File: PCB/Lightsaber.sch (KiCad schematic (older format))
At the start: 10 parts, among them Q1 SS8050, Q2 SS8050, Q3 SS8050, SW1 SW_Push

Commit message: updated ss8050 pin numbering
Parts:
- D2: footprint (none) -> Connector_PinHeader_2.54mm:PinHeader_1x04_P2.54mm_Vertical
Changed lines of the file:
@@
 F 0 "D2" V 10196 820 50  0000 R CNN
 F 1 "LED_ARGB" V 10105 820 50  0000 R CNN
-F 2 "" H 10150 1100 50  0001 C CNN
+F 2 "Connector_PinHeader_2.54mm:PinHeader_1x04_P2.54mm_Vertical" H 10150 1100 50  0001 C CNN
 F 3 "~" H 10150 1100 50  0001 C CNN
 	1    10150 1150

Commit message: update
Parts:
- added BT?: Battery_Cell, symbol Device:Battery_Cell
- added C?: C, symbol Device:C
- added F?: Fuse, symbol Device:Fuse
- added R?: 100, symbol Device:R
- added U?: DW01A, symbol Lightsaber_custom:DW01A
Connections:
- new net: BT?.1 (+), F?.2
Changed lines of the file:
@@
 Wire Wire Line
 	9800 3250 9800 3400
+$Comp
+L Device:Battery_Cell BT?
+U 1 1 631E3320
+P 800 1800
+F 0 "BT?" H 918 1896 50  0000 L CNN
+F 1 "Battery_Cell" H 918 1805 50  0000 L CNN
+F 2 "" V 800 1860 50  0001 C CNN
+F 3 "~" V 800 1860 50  0001 C CNN
+	1    800  1800
+	1    0    0    -1
+$EndComp
+$Comp
+L Device:Fuse F?
+U 1 1 631E4D50
+P 1200 1550
+F 0 "F?" V 1003 1550 50  0000 C CNN
+F 1 "Fuse" V 1094 1550 50  0000 C CNN
+F 2 "" V 1130 1550 50  0001 C CNN
+F 3 "~" H 1200 1550 50  0001 C CNN
+	1    1200 1550
+	0    1    1    0
+$EndComp
+Wire Wire Line
+	800  1600 800  1550
+Wire Wire Line
+	800  1550 1050 1550
+$Comp
+L Lightsaber_custom:DW01A U?
+U 1 1 631E6E9D
+P 2800 1150
+F 0 "U?" H 2750 1215 50  0000 C CNN
+F 1 "DW01A" H 2750 1124 50  0000 C CNN
+F 2 "" H 2750 1200 50  0001 C CNN
+F 3 "" H 2750 1200 50  0001 C CNN
+	1    2800 1150
+	1    0    0    -1
+$EndComp
+$Comp
+L Device:R R?
+U 1 1 631E7B9E
+P 1900 1350
+F 0 "R?" V 1693 1350 50  0000 C CNN
+F 1 "100" V 1784 1350 50  0000 C CNN
+F 2 "" V 1830 1350 50  0001 C CNN
+F 3 "~" H 1900 1350 50  0001 C CNN
+	1    1900 1350
+	0    1    1    0
+$EndComp
+$Comp
+L Device:C C?
+U 1 1 631E8406
+P 2100 1650
+F 0 "C?" H 2215 1696 50  0000 L CNN
+F 1 "C" H 2215 1605 50  0000 L CNN
+F 2 "" H 2138 1500 50  0001 C CNN
+F 3 "~" H 2100 1650 50  0001 C CNN
+	1    2100 1650
+	1    0    0    -1
+$EndComp
 $EndSCHEMATC

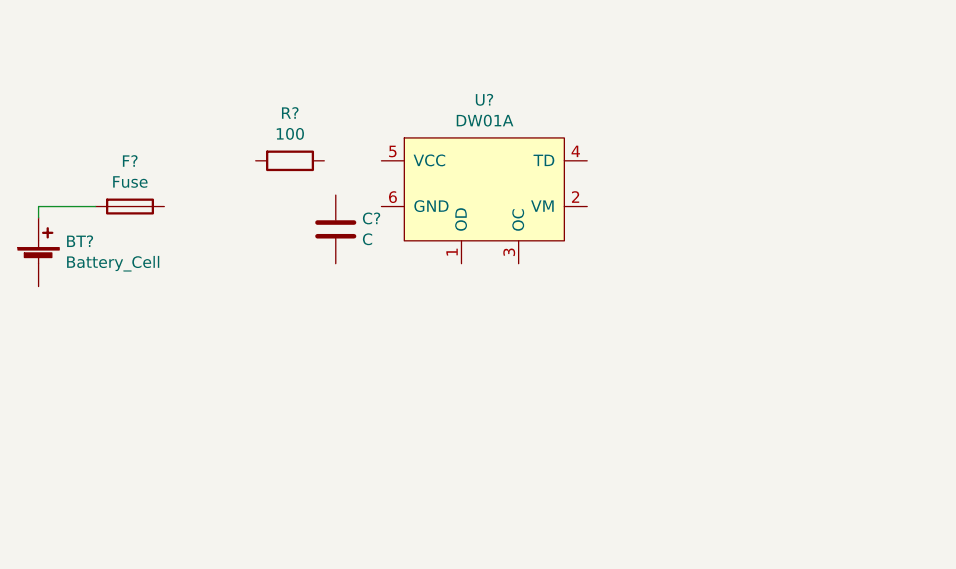
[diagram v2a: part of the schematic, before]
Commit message: battery protection added
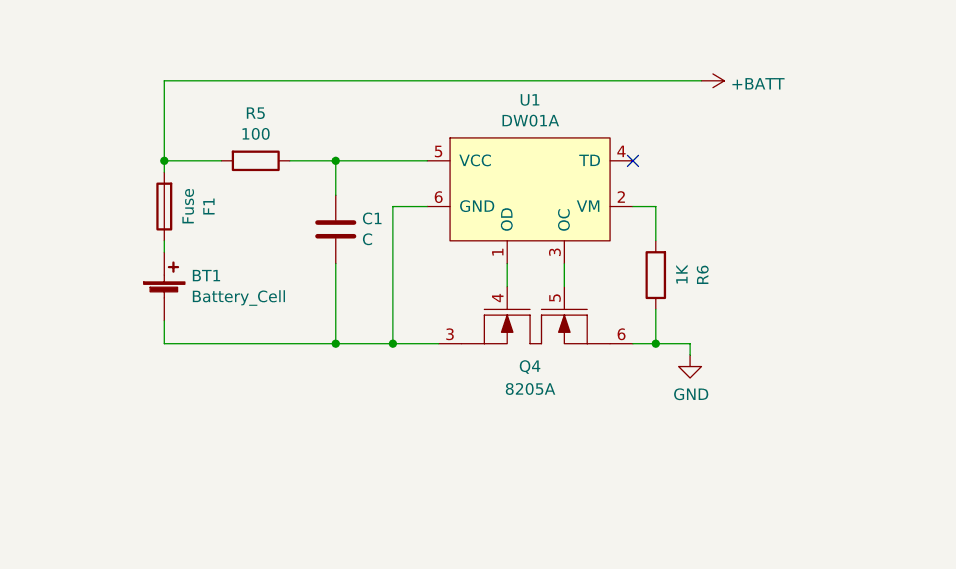
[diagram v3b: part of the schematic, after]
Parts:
- added Q4: 8205A, Package_SO:TSSOP-8_4.4x3mm_P0.65mm, symbol Lightsaber_custom:8205A
- added R6: 1K, Resistor_SMD:R_0402_1005Metric, symbol Device:R
- R5: renamed from R?; footprint (none) -> Resistor_SMD:R_0402_1005Metric
- U1: renamed from U?; footprint (none) -> Package_TO_SOT_SMD:SOT-23-6_Handsoldering
- gave numbers to parts that had none: 3
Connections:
- net GND: now also Q4.6 (S2), R6.1
- net at BT1.1 (+): now also F1.1; no longer F1.2
- net at BT1.2 (-): now also C1.2, U1.6 (GND), Q4.3 (S1)
- net at U1.1 (OD): now also Q4.4 (G1)
- net at U1.2 (VM): now also R6.2
- net at U1.3 (OC): now also Q4.5 (G2)
- net at U1.5 (VCC): now also C1.1, R5.1
- net +BATT: now reaches R5.2
- net +BATT: now also F1.2
- no-connect marks 0 -> 1
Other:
- moved on the sheet: BT1, F1, R5, U1
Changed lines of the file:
@@
 	9800 3250 9800 3400
 $Comp
-L Device:Battery_Cell BT?
+L Device:Battery_Cell BT1
 U 1 1 631E3320
-P 800 1800
-F 0 "BT?" H 918 1896 50  0000 L CNN
-F 1 "Battery_Cell" H 918 1805 50  0000 L CNN
-F 2 "" V 800 1860 50  0001 C CNN
-F 3 "~" V 800 1860 50  0001 C CNN
-	1    800  1800
+P 1350 1950
+F 0 "BT1" H 1468 2046 50  0000 L CNN
+F 1 "Battery_Cell" H 1468 1955 50  0000 L CNN
+F 2 "" V 1350 2010 50  0001 C CNN
+F 3 "~" V 1350 2010 50  0001 C CNN
+	1    1350 1950
 	1    0    0    -1
 $EndComp
 $Comp
-L Device:Fuse F?
+L Device:Fuse F1
 U 1 1 631E4D50
-P 1200 1550
-F 0 "F?" V 1003 1550 50  0000 C CNN
-F 1 "Fuse" V 1094 1550 50  0000 C CNN
-F 2 "" V 1130 1550 50  0001 C CNN
-F 3 "~" H 1200 1550 50  0001 C CNN
-	1    1200 1550
-	0    1    1    0
+P 1350 1550
+F 0 "F1" V 1153 1550 50  0000 C CNN
+F 1 "Fuse" V 1244 1550 50  0000 C CNN
+F 2 "" V 1280 1550 50  0001 C CNN
+F 3 "~" H 1350 1550 50  0001 C CNN
+	1    1350 1550
+	-1   0    0    1
 $EndComp
-Wire Wire Line
-	800  1600 800  1550
-Wire Wire Line
-	800  1550 1050 1550
 $Comp
-L Lightsaber_custom:DW01A U?
+L Lightsaber_custom:DW01A U1
 U 1 1 631E6E9D
-P 2800 1150
-F 0 "U?" H 2750 1215 50  0000 C CNN
-F 1 "DW01A" H 2750 1124 50  0000 C CNN
-F 2 "" H 2750 1200 50  0001 C CNN
-F 3 "" H 2750 1200 50  0001 C CNN
-	1    2800 1150
+P 3000 1150
+F 0 "U1" H 2950 1215 50  0000 C CNN
+F 1 "DW01A" H 2950 1124 50  0000 C CNN
+F 2 "Package_TO_SOT_SMD:SOT-23-6_Handsoldering" H 2950 1200 50  0001 C CNN
+F 3 "" H 2950 1200 50  0001 C CNN
+	1    3000 1150
 	1    0    0    -1
 $EndComp
 $Comp
-L Device:R R?
+L Device:R R5
 U 1 1 631E7B9E
-P 1900 1350
-F 0 "R?" V 1693 1350 50  0000 C CNN
-F 1 "100" V 1784 1350 50  0000 C CNN
-F 2 "" V 1830 1350 50  0001 C CNN
-F 3 "~" H 1900 1350 50  0001 C CNN
-	1    1900 1350
+P 1750 1350
+F 0 "R5" V 1543 1350 50  0000 C CNN
+F 1 "100" V 1634 1350 50  0000 C CNN
+F 2 "Resistor_SMD:R_0402_1005Metric" V 1680 1350 50  0001 C CNN
+F 3 "~" H 1750 1350 50  0001 C CNN
+	1    1750 1350
 	0    1    1    0
 $EndComp
 $Comp
-L Device:C C?
+L Device:C C1
 U 1 1 631E8406
 P 2100 1650
-F 0 "C?" H 2215 1696 50  0000 L CNN
+F 0 "C1" H 2215 1696 50  0000 L CNN
 F 1 "C" H 2215 1605 50  0000 L CNN
 F 2 "" H 2138 1500 50  0001 C CNN
@@
 	1    0    0    -1
 $EndComp
+$Comp
+L power:GND #PWR0101
+U 1 1 631F39B5
+P 3650 2200
+F 0 "#PWR0101" H 3650 1950 50  0001 C CNN
+F 1 "GND" H 3655 2027 50  0000 C CNN
+F 2 "" H 3650 2200 50  0001 C CNN
+F 3 "" H 3650 2200 50  0001 C CNN
+	1    3650 2200
+	1    0    0    -1
+$EndComp
+$Comp
+L Lightsaber_custom:8205A Q4
+U 1 1 631FA975
+P 3000 1700
+F 0 "Q4" H 2950 1150 50  0000 C CNN
+F 1 "8205A" H 2950 1050 50  0000 C CNN
+F 2 "Package_SO:TSSOP-8_4.4x3mm_P0.65mm" H 3000 1700 50  0001 C CNN
+F 3 "" H 3000 1700 50  0001 C CNN
+	1    3000 1700
+	1    0    0    -1
+$EndComp
+Wire Wire Line
+	2850 1800 2850 1900
+Wire Wire Line
+	3100 1800 3100 1900
+Wire Wire Line
+	2500 1550 2350 1550
+Wire Wire Line
+	2350 1550 2350 2150
+Connection ~ 2350 2150
+Wire Wire Line
+	2350 2150 2550 2150
+Wire Wire Line
+	2500 1350 2100 1350
+Wire Wire Line
+	2100 1500 2100 1350
+Connection ~ 2100 1350
+Wire Wire Line
+	2100 1350 1900 1350
+Wire Wire Line
+	2100 1800 2100 2150
+Wire Wire Line
+	2100 2150 2350 2150
+Wire Wire Line
+	1350 1350 1350 1400
+Wire Wire Line
+	1350 1700 1350 1750
+Wire Wire Line
+	1350 1350 1600 1350
+Wire Wire Line
+	1350 2050 1350 2150
+Connection ~ 2100 2150
+Wire Wire Line
+	3650 2200 3650 2150
+Wire Wire Line
+	1350 2150 2100 2150
+$Comp
+L Device:R R6
+U 1 1 6320AF5C
+P 3500 1850
+F 0 "R6" V 3293 1850 50  0000 C CNN
+F 1 "1K" V 3384 1850 50  0000 C CNN
+F 2 "Resistor_SMD:R_0402_1005Metric" V 3430 1850 50  0001 C CNN
+F 3 "~" H 3500 1850 50  0001 C CNN
+	1    3500 1850
+	-1   0    0    1
+$EndComp
+Wire Wire Line
+	3400 2150 3500 2150
+Wire Wire Line
+	3500 2000 3500 2150
+Connection ~ 3500 2150
+Wire Wire Line
+	3500 2150 3650 2150
+Wire Wire Line
+	3500 1700 3500 1550
+Wire Wire Line
+	3500 1550 3400 1550
+NoConn ~ 3400 1350
+Wire Wire Line
+	1350 1350 1350 1000
+Wire Wire Line
+	1350 1000 3700 1000
+Connection ~ 1350 1350
+$Comp
+L power:+BATT #PWR0102
+U 1 1 6321023C
+P 3700 1000
+F 0 "#PWR0102" H 3700 850 50  0001 C CNN
+F 1 "+BATT" V 3715 1128 50  0000 L CNN
+F 2 "" H 3700 1000 50  0001 C CNN
+F 3 "" H 3700 1000 50  0001 C CNN
+	1    3700 1000
+	0    1    1    0
+$EndComp
 $EndSCHEMATC

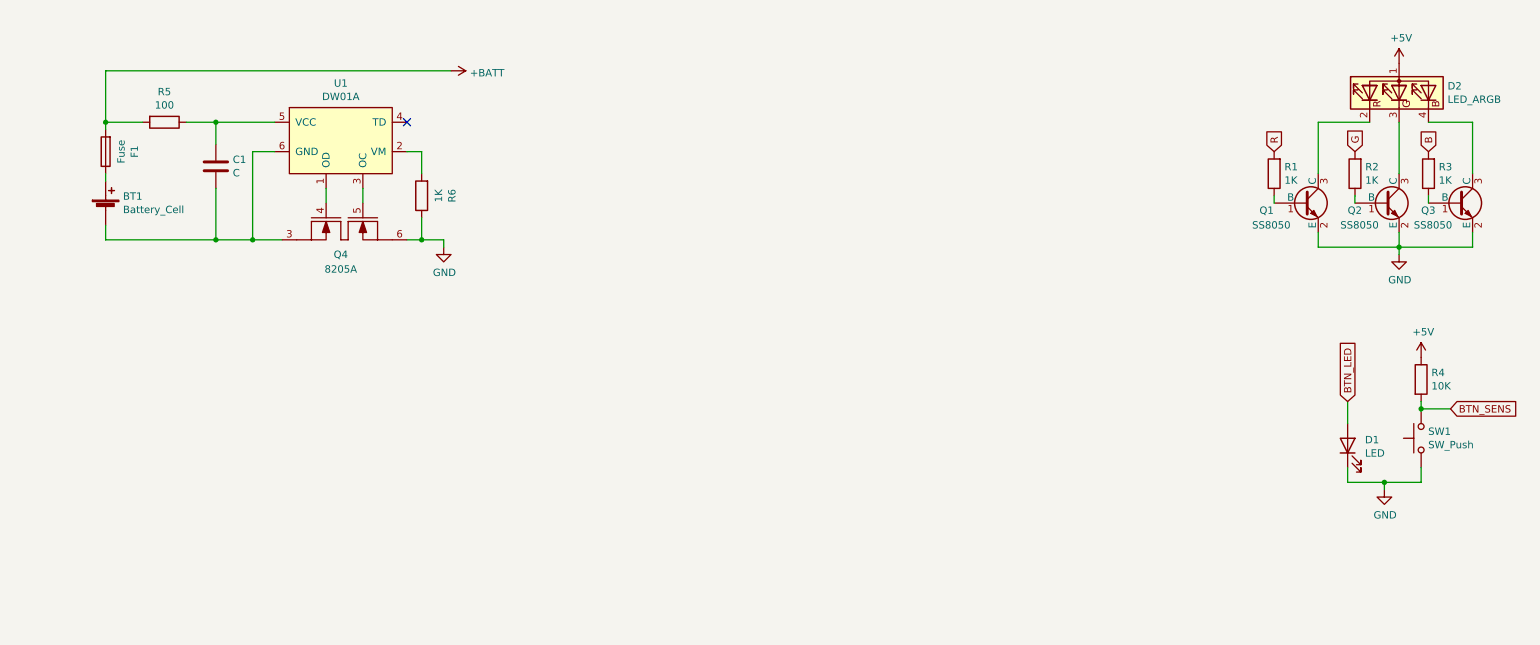
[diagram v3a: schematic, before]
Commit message: charging circuit added
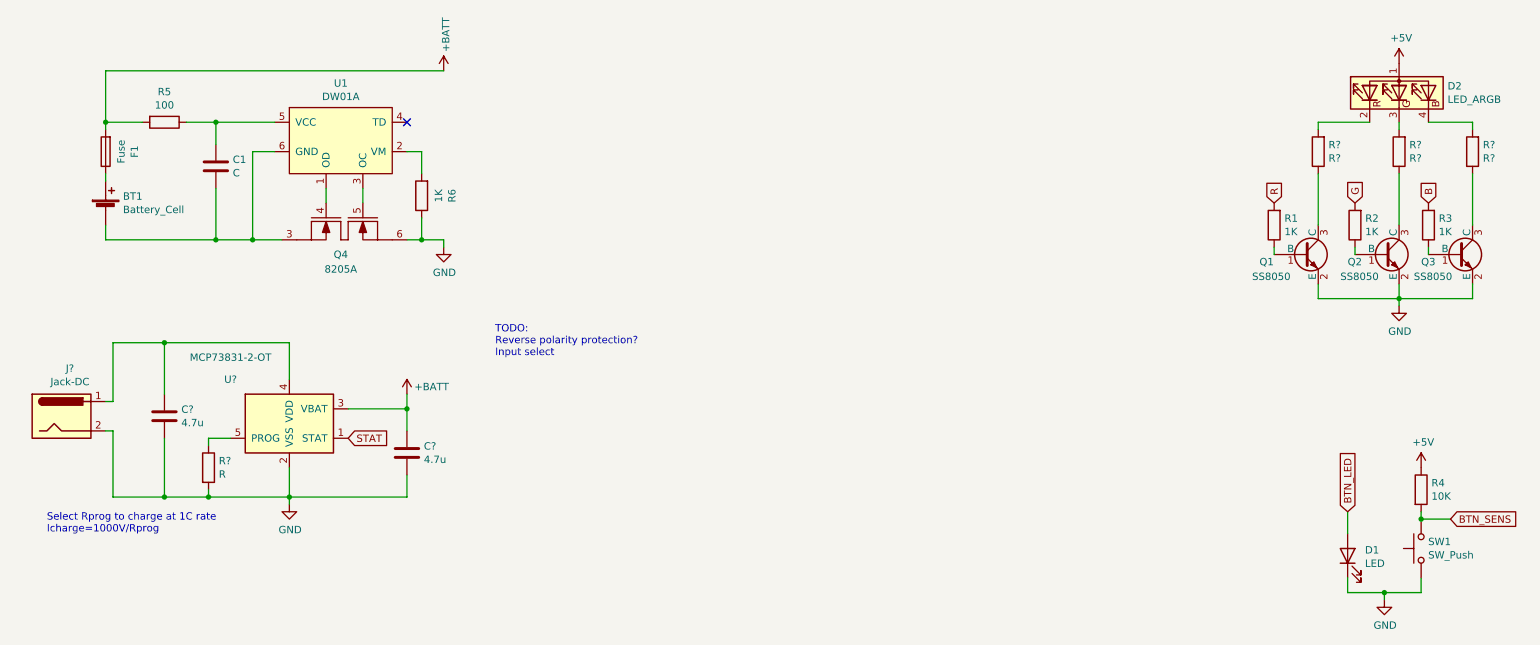
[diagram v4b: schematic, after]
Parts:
- added C? (x2): 4.7u, symbol Device:C
- added J?: Jack-DC, symbol Connector:Jack-DC
- added R?: R, symbol Device:R
- added R? (x3): R?, Resistor_SMD:R_0402_1005Metric, symbol Device:R
- added U?: MCP73831-2-OT, Package_TO_SOT_SMD:SOT-23-5, symbol Battery_Management:MCP73831-2-OT
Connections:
- net +BATT: now also C?.1, U?.3 (VBAT)
- net GND: now also C?.2, C?.2, J?.2, R?.2, U?.2 (VSS)
- net at Q1.3 (C): now also R?.1; no longer D2.2 (RK)
- net at D2.3 (GK): now also R?.2; no longer Q2.3 (C)
- net at D2.4 (BK): now also R?.2; no longer Q3.3 (C)
- new net: D2.2 (RK), R?.2
- new net: Q2.3 (C), R?.1
- new net: Q3.3 (C), R?.1
- new net: C?.1, J?.1, U?.4 (VDD)
- new net: R?.1, U?.5 (PROG)
- new net STAT: U?.1 (STAT)
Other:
- note added: "Select Rprog to charge at 1C rate\nIcharge=1000V/Rprog"
- note added: "TODO:\nReverse polarity protection?\nInput select"
- moved on the sheet: D1, Q1, Q2, Q3, R1, R2, R3, R4, SW1

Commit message: input power select added
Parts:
- added D?: D_Schottky, symbol Device:D_Schottky
- added Q?: AO3401A, Package_TO_SOT_SMD:SOT-23, symbol Transistor_FET:AO3401A
- added R?: 10K, Resistor_SMD:R_0402_1005Metric, symbol Device:R
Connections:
- net +BATT: now also Q?.2 (S); no longer U?.3 (VBAT)
- net GND: now also R?.1
- net at C?.1, J?.1, U?.4 (VDD): now also D?.2 (A), Q?.1 (G), R?.2
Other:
- note added: "TODO:\nReverse polarity protection?"
- note removed: "TODO:\nReverse polarity protection?\nInput select"
- moved on the sheet: C?
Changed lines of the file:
@@
 U 1 1 631F6B34
 P 2600 3400
-F 0 "U?" H 2200 3700 50  0000 C CNN
-F 1 "MCP73831-2-OT" H 2200 3850 50  0000 C CNN
+F 0 "U?" H 2850 3750 50  0000 C CNN
+F 1 "MCP73831-2-OT" H 3050 3900 50  0000 C CNN
 F 2 "Package_TO_SOT_SMD:SOT-23-5" H 2650 3150 50  0001 L CIN
 F 3 "http://ww1.microchip.com/downloads/en/DeviceDoc/20001984g.pdf" H 2450 3350 50  0001 C CNN
@@
 Wire Wire Line
 	1750 3500 1750 3900
-Wire Wire Line
-	2600 2850 2600 3100
-Wire Wire Line
-	1750 3200 1750 2850
 $Comp
 L power:+BATT #PWR?
 U 1 1 6320727D
-P 3400 3200
-F 0 "#PWR?" H 3400 3050 50  0001 C CNN
-F 1 "+BATT" H 3450 3250 50  0000 L CNN
-F 2 "" H 3400 3200 50  0001 C CNN
-F 3 "" H 3400 3200 50  0001 C CNN
-	1    3400 3200
+P 3250 3200
+F 0 "#PWR?" H 3250 3050 50  0001 C CNN
+F 1 "+BATT" H 3300 3250 50  0000 L CNN
+F 2 "" H 3250 3200 50  0001 C CNN
+F 3 "" H 3250 3200 50  0001 C CNN
+	1    3250 3200
 	1    0    0    -1
 $EndComp
@@
 Connection ~ 2600 3900
 Wire Wire Line
-	1750 2850 2600 2850
+	1750 2750 2600 2750
 Wire Wire Line
 	1750 3900 2050 3900
@@
 	1350 3250 1400 3250
 Wire Wire Line
-	1400 3250 1400 2850
-Wire Wire Line
-	1400 2850 1750 2850
-Connection ~ 1750 2850
+	1400 2750 1750 2750
+Connection ~ 1750 2750
 Wire Wire Line
 	1350 3450 1400 3450
@@
 Connection ~ 1750 3900
 Wire Wire Line
-	3400 3750 3400 3900
-Wire Wire Line
-	3400 3200 3400 3300
-Connection ~ 3400 3300
-Wire Wire Line
-	3400 3300 3400 3450
-Text GLabel 3000 3500 2    50   Input ~ 0
+	3250 3750 3250 3900
+Wire Wire Line
+	3250 3200 3250 3300
+Connection ~ 3250 3300
+Wire Wire Line
+	3250 3300 3250 3450
+Text GLabel 3050 3550 3    50   Input ~ 0
 STAT
 $Comp
 L Device:C C?
 U 1 1 63203FE4
-P 3400 3600
-F 0 "C?" H 3515 3646 50  0000 L CNN
-F 1 "4.7u" H 3515 3555 50  0000 L CNN
-F 2 "" H 3438 3450 50  0001 C CNN
-F 3 "~" H 3400 3600 50  0001 C CNN
-	1    3400 3600
-	1    0    0    -1
-$EndComp
-Wire Wire Line
-	3000 3300 3400 3300
-Wire Wire Line
-	2600 3900 3400 3900
-Text Notes 4000 2950 0    50   ~ 0
-TODO:\nReverse polarity protection?\nInput select
+P 3250 3600
+F 0 "C?" H 3365 3646 50  0000 L CNN
+F 1 "4.7u" H 3365 3555 50  0000 L CNN
+F 2 "" H 3288 3450 50  0001 C CNN
+F 3 "~" H 3250 3600 50  0001 C CNN
+	1    3250 3600
+	1    0    0    -1
+$EndComp
+Text Notes 800  2600 0    50   ~ 0
+TODO:\nReverse polarity protection?
 $Comp
 L Device:R R?
@@
 Wire Wire Line
 	10650 1350 10650 1400
+$Comp
+L Transistor_FET:AO3401A Q?
+U 1 1 63207EF7
+P 4150 3200
+F 0 "Q?" V 4399 3200 50  0000 C CNN
+F 1 "AO3401A" V 4490 3200 50  0000 C CNN
+F 2 "Package_TO_SOT_SMD:SOT-23" H 4350 3125 50  0001 L CIN
+F 3 "http://www.aosmd.com/pdfs/datasheet/AO3401A.pdf" H 4150 3200 50  0001 L CNN
+	1    4150 3200
+	0    1    1    0
+$EndComp
+$Comp
+L Device:R R?
+U 1 1 6320D8B1
+P 3700 2900
+F 0 "R?" V 3493 2900 50  0000 C CNN
+F 1 "10K" V 3584 2900 50  0000 C CNN
+F 2 "Resistor_SMD:R_0402_1005Metric" V 3630 2900 50  0001 C CNN
+F 3 "~" H 3700 2900 50  0001 C CNN
+	1    3700 2900
+	-1   0    0    1
+$EndComp
+Wire Wire Line
+	3700 2750 4150 2750
+$Comp
+L power:GND #PWR?
+U 1 1 632145C1
+P 3700 3050
+F 0 "#PWR?" H 3700 2800 50  0001 C CNN
+F 1 "GND" H 3705 2877 50  0000 C CNN
+F 2 "" H 3700 3050 50  0001 C CNN
+F 3 "" H 3700 3050 50  0001 C CNN
+	1    3700 3050
+	1    0    0    -1
+$EndComp
+Wire Wire Line
+	1400 2750 1400 3250
+Wire Wire Line
+	1750 2750 1750 3200
+Wire Wire Line
+	2600 2750 2600 3100
+Wire Wire Line
+	4150 2750 4150 3000
+Wire Wire Line
+	3950 3300 3250 3300
+$Comp
+L Device:D_Schottky D?
+U 1 1 63223B80
+P 4700 2750
+F 0 "D?" H 4700 2533 50  0000 C CNN
+F 1 "D_Schottky" H 4700 2624 50  0000 C CNN
+F 2 "" H 4700 2750 50  0001 C CNN
+F 3 "~" H 4700 2750 50  0001 C CNN
+	1    4700 2750
+	-1   0    0    1
+$EndComp
+Wire Wire Line
+	4550 2750 4150 2750
+Connection ~ 4150 2750
+Wire Wire Line
+	3050 3550 3050 3500
+Wire Wire Line
+	3050 3500 3000 3500
+Wire Wire Line
+	3250 3900 2600 3900
+Wire Wire Line
+	2600 2750 3700 2750
+Connection ~ 2600 2750
+Connection ~ 3700 2750
 $EndSCHEMATC
